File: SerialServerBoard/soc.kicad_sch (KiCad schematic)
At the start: 21 parts, among them U1 SG2002

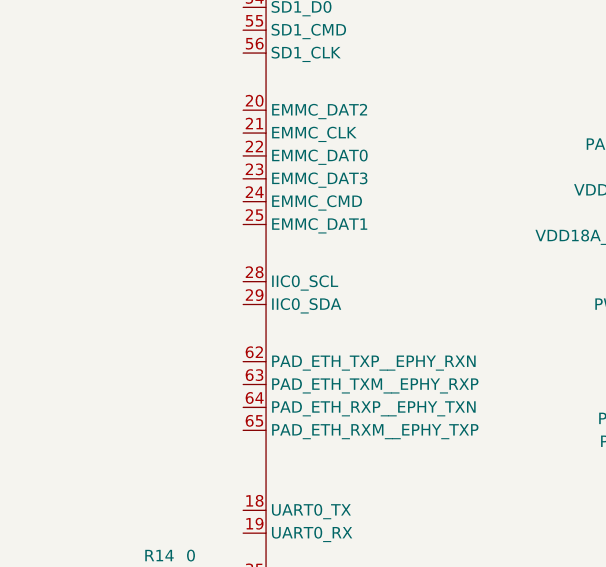
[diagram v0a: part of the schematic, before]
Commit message: Add ATECC
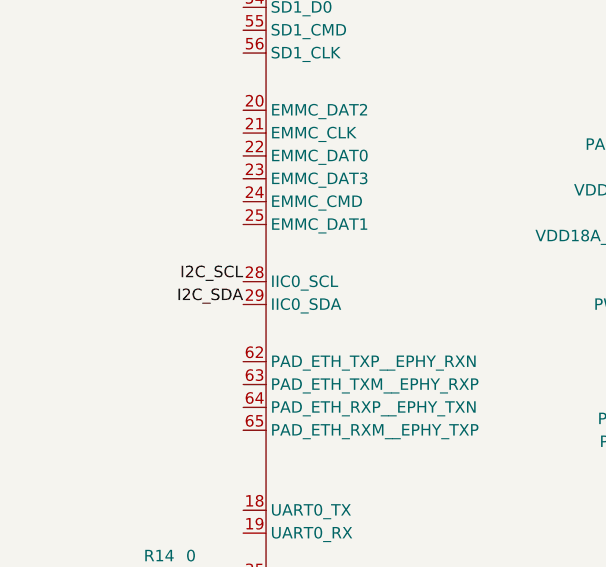
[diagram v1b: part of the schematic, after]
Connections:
- net I2C_SCL: now reaches U1.28 (IIC0_SCL)
- net I2C_SDA: now reaches U1.29 (IIC0_SDA)
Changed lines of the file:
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@@
+		)
+	)
+	(label "I2C_SDA"
+		(at 88.9 88.9 180)
+		(fields_autoplaced yes)
+		(effects
+			(font
+				(size 1.27 1.27)
+			)
+			(justify right bottom)
+		)
+	)
+	(label "I2C_SCL"
+		(at 88.9 86.36 180)
+		(fields_autoplaced yes)
+		(effects
+			(font
+				(size 1.27 1.27)
+			)
+			(justify right bottom)
 		)
 	)

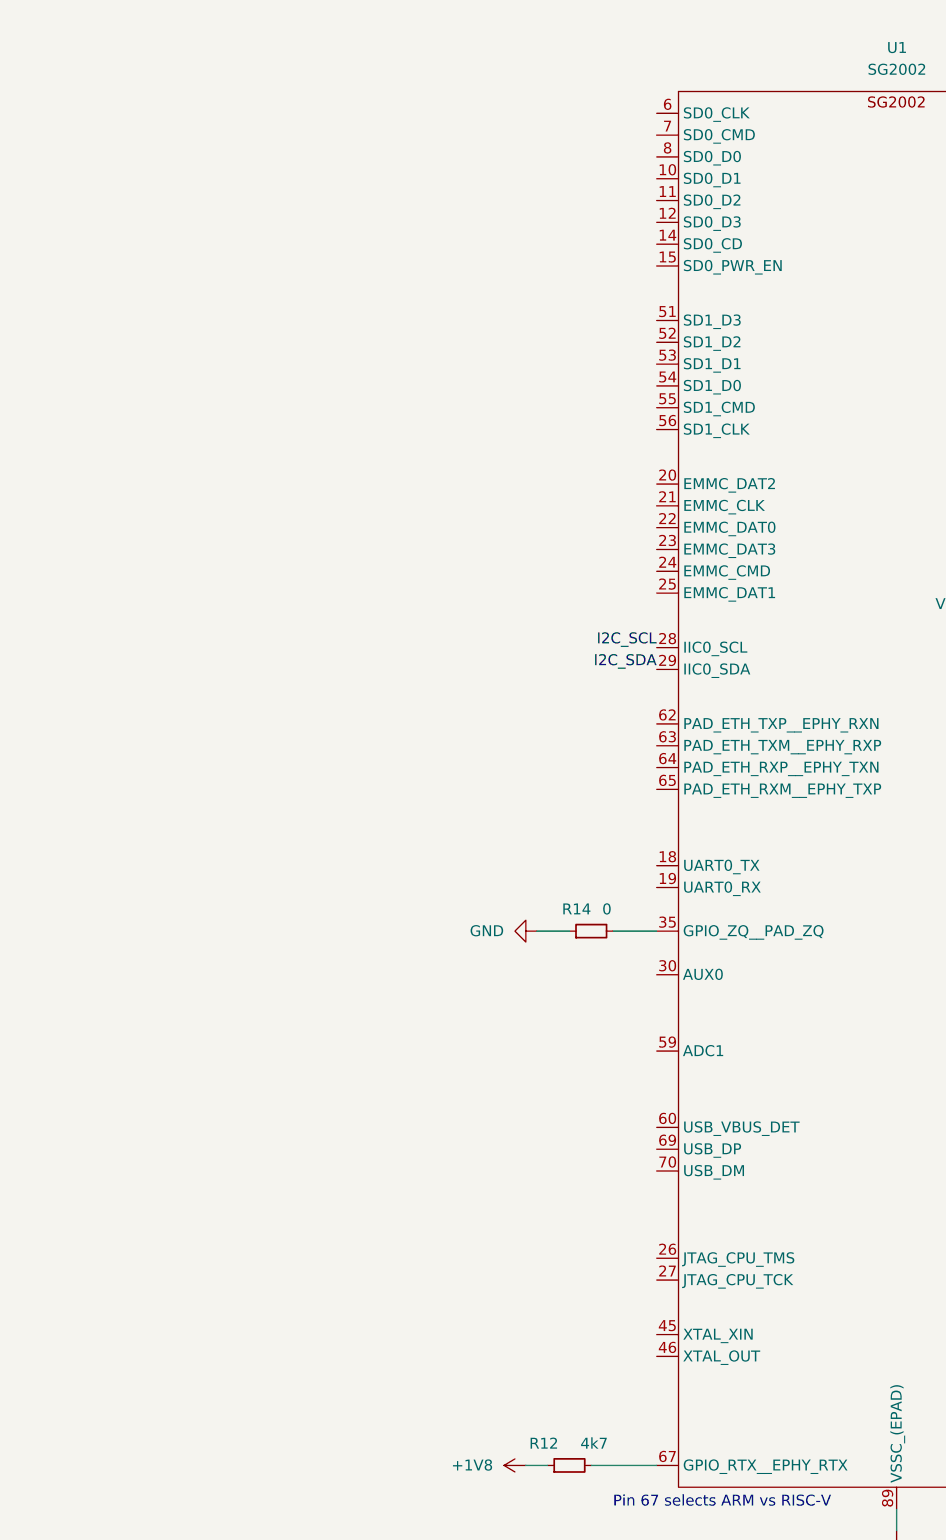
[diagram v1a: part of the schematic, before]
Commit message: Add micro-SD card slot
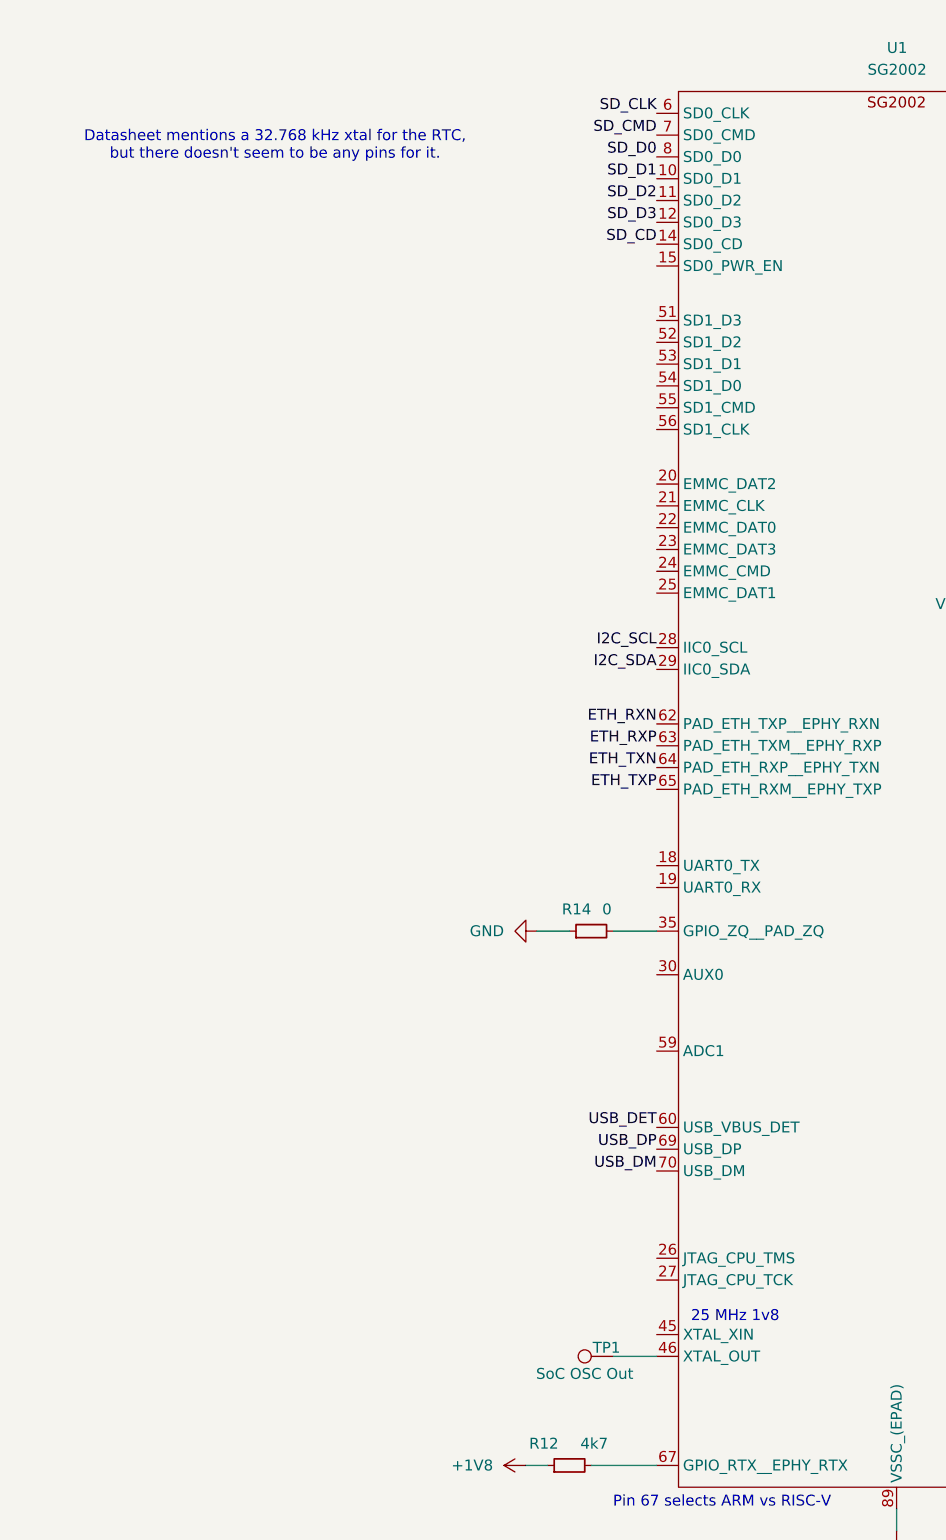
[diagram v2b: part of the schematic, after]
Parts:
- added TP1: SoC OSC Out, symbol Connector:TestPoint
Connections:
- net SD_D1: now reaches U1.10 (SD0_D1)
- net SD_D2: now reaches U1.11 (SD0_D2)
- net SD_D3: now reaches U1.12 (SD0_D3)
- net SD_CD: now reaches U1.14 (SD0_CD)
- net at U1.46 (XTAL_OUT): now also TP1.1
- net SD_CLK: now reaches U1.6 (SD0_CLK)
- net USB_DET: now reaches U1.60 (USB_VBUS_DET)
- net ETH_RXN: now reaches U1.62 (PAD_ETH_TXP__EPHY_RXN)
- net ETH_RXP: now reaches U1.63 (PAD_ETH_TXM__EPHY_RXP)
- net ETH_TXN: now reaches U1.64 (PAD_ETH_RXP__EPHY_TXN)
- net ETH_TXP: now reaches U1.65 (PAD_ETH_RXM__EPHY_TXP)
- net USB_DP: now reaches U1.69 (USB_DP)
- net SD_CMD: now reaches U1.7 (SD0_CMD)
- net USB_DM: now reaches U1.70 (USB_DM)
- net SD_D0: now reaches U1.8 (SD0_D0)
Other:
- note added: "25 MHz 1v8"
- note added: "Datasheet mentions a 32.768 kHz xtal for the RTC, but there doesn't seem to be any pins for it."
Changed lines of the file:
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@@
+	(wire
+		(pts
+			(xy 83.82 168.91) (xy 88.9 168.91)
+		)
+		(stroke
+			(width 0)
+			(type default)
+		)
+	)
 	(wire
 		(pts
@@
 		)
 	)
+	(text "Datasheet mentions a 32.768 kHz xtal for the RTC,\nbut there doesn't seem to be any pins for it."
+		(exclude_from_sim no)
+		(at 44.45 27.94 0)
+		(effects
+			(font
+				(size 1.27 1.27)
+			)
+		)
+	)
 	(text "Duo 256M has PWR_VBAT_DET on voltage divider:\n 3v3 - 4.7k - PWR_VBAT_DET - 3.3k - GND\n Pin is pulled to ground when a RUN pin goes high - probably a disable/reset pin"
 		(exclude_from_sim no)
@@
 		)
 	)
+	(text "25 MHz 1v8"
+		(exclude_from_sim no)
+		(at 98.044 164.338 0)
+		(effects
+			(font
+				(size 1.27 1.27)
+			)
+		)
+	)
 	(text "VCORE = 0.9V"
 		(exclude_from_sim no)
@@
 		)
 	)
+	(label "SD_CMD"
+		(at 88.9 26.67 180)
+		(fields_autoplaced yes)
+		(effects
+			(font
+				(size 1.27 1.27)
+			)
+			(justify right bottom)
+		)
+	)
 	(label "I2C_SDA"
 		(at 88.9 88.9 180)
@@
 		)
 	)
+	(label "USB_DET"
+		(at 88.9 142.24 180)
+		(fields_autoplaced yes)
+		(effects
+			(font
+				(size 1.27 1.27)
+			)
+			(justify right bottom)
+		)
+	)
+	(label "USB_DM"
+		(at 88.9 147.32 180)
+		(fields_autoplaced yes)
+		(effects
+			(font
+				(size 1.27 1.27)
+			)
+			(justify right bottom)
+		)
+	)
+	(label "ETH_RXN"
+		(at 88.9 95.25 180)
+		(fields_autoplaced yes)
+		(effects
+			(font
+				(size 1.27 1.27)
+			)
+			(justify right bottom)
+		)
+	)
+	(label "SD_D1"
+		(at 88.9 31.75 180)
+		(fields_autoplaced yes)
+		(effects
+			(font
+				(size 1.27 1.27)
+			)
+			(justify right bottom)
+		)
+	)
+	(label "USB_DP"
+		(at 88.9 144.78 180)
+		(fields_autoplaced yes)
+		(effects
+			(font
+				(size 1.27 1.27)
+			)
+			(justify right bottom)
+		)
+	)
 	(label "I2C_SCL"
 		(at 88.9 86.36 180)
+		(fields_autoplaced yes)
+		(effects
+			(font
+				(size 1.27 1.27)
+			)
+			(justify right bottom)
+		)
+	)
+	(label "SD_CD"
+		(at 88.9 39.37 180)
+		(fields_autoplaced yes)
+		(effects
+			(font
+				(size 1.27 1.27)
+			)
+			(justify right bottom)
+		)
+	)
+	(label "SD_CLK"
+		(at 88.9 24.13 180)
+		(fields_autoplaced yes)
+		(effects
+			(font
+				(size 1.27 1.27)
+			)
+			(justify right bottom)
+		)
+	)
+	(label "ETH_TXP"
+		(at 88.9 102.87 180)
+		(fields_autoplaced yes)
+		(effects
+			(font
+				(size 1.27 1.27)
+			)
+			(justify right bottom)
+		)
+	)
+	(label "ETH_RXP"
+		(at 88.9 97.79 180)
+		(fields_autoplaced yes)
+		(effects
+			(font
+				(size 1.27 1.27)
+			)
+			(justify right bottom)
+		)
+	)
+	(label "SD_D0"
+		(at 88.9 29.21 180)
+		(fields_autoplaced yes)
+		(effects
+			(font
+				(size 1.27 1.27)
+			)
+			(justify right bottom)
+		)
+	)
+	(label "ETH_TXN"
+		(at 88.9 100.33 180)
+		(fields_autoplaced yes)
+		(effects
+			(font
+				(size 1.27 1.27)
+			)
+			(justify right bottom)
+		)
+	)
+	(label "SD_D2"
+		(at 88.9 34.29 180)
+		(fields_autoplaced yes)
+		(effects
+			(font
+				(size 1.27 1.27)
+			)
+			(justify right bottom)
+		)
+	)
+	(label "SD_D3"
+		(at 88.9 36.83 180)
 		(fields_autoplaced yes)
 		(effects
@@
 					(unit 1)
 				)
+			)
+		)
+	)
+	(symbol
+		(lib_id "Connector:TestPoint")
+		(at 83.82 168.91 90)
+		(unit 1)
+		(exclude_from_sim no)
+		(in_bom yes)
+		(on_board yes)
+		(dnp no)
+		(property "Reference" "TP1"
+			(at 83.058 167.894 90)
+			(effects
+				(font
+					(size 1.27 1.27)
+				)
+			)
+		)
+		(property "Value" "SoC OSC Out"
+			(at 80.518 170.942 90)
+			(effects
+				(font
+					(size 1.27 1.27)
+				)
+			)
+		)
+		(property "Footprint" ""
+			(at 83.82 163.83 0)
+			(effects
+				(font
+					(size 1.27 1.27)
+				)
+				(hide yes)
+			)
+		)
+		(property "Datasheet" "~"
+			(at 83.82 163.83 0)
+			(effects
+				(font
+					(size 1.27 1.27)
+				)
+				(hide yes)
+			)
+		)
+		(property "Description" "test point"
+			(at 83.82 168.91 0)
+			(effects
+				(font
+					(size 1.27 1.27)
+				)
+				(hide yes)
+			)
+		)
+		(pin "1"
+		)
+		(instances
+			(project "SerialServerBoard"
+				(path "/fff4edd7-7765-4881-b8c8-325c8be7c8ba/70988b15-c4e0-4a4b-8c11-4e6331245de1"
+					(reference "TP1")
+					(unit 1)
+				)
